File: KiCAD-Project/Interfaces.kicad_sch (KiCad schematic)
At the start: 62 parts, among them J201 XT30, J202 Conn_02x04_Odd_Even, J203 Conn_01x03_Shielded, J204 Conn_01x03_Shielded, U201 TI_TCAN337G, U202 TLE5012B_E1000, U203 MAX15062A

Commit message: fixing DRC
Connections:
- net +3V3: now also J202.8 (Pin_8); no longer J202.1 (Pin_1)
- net ENCODER_CS1: now also J202.2 (Pin_2); no longer J202.7 (Pin_7)
- net ENCODER_DATA: now also J202.6 (Pin_6); no longer J202.3 (Pin_3)
- net ENCODER_QOAD_A2: now also J202.5 (Pin_5); no longer J202.4 (Pin_4)
- net ENCODER_QOAD_B2: now also J202.3 (Pin_3); no longer J202.6 (Pin_6)
- net ENCODER_QOAD_I2: now also J202.1 (Pin_1); no longer J202.8 (Pin_8)
- net ENCODER_SCK: now also J202.4 (Pin_4); no longer J202.5 (Pin_5)
- net GNDS: now also J202.7 (Pin_7); no longer J202.2 (Pin_2)
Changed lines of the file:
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@@
   (junction (at 254 133.35) (diameter 1.016) (color 0 0 0 0))
   (junction (at 259.08 82.55) (diameter 1.016) (color 0 0 0 0))
-  (junction (at 262.89 128.27) (diameter 1.016) (color 0 0 0 0))
-  (junction (at 265.43 130.81) (diameter 1.016) (color 0 0 0 0))
+  (junction (at 262.89 130.81) (diameter 1.016) (color 0 0 0 0))
+  (junction (at 265.43 128.27) (diameter 1.016) (color 0 0 0 0))
   (junction (at 266.7 120.65) (diameter 1.016) (color 0 0 0 0))
-  (junction (at 267.97 149.86) (diameter 1.016) (color 0 0 0 0))
+  (junction (at 267.97 157.48) (diameter 1.016) (color 0 0 0 0))
   (junction (at 280.67 118.11) (diameter 1.016) (color 0 0 0 0))
   (junction (at 289.56 77.47) (diameter 1.016) (color 0 0 0 0))
@@
     (stroke (width 0) (type solid) (color 0 0 0 0))
   )
-  (wire (pts (xy 248.92 128.27) (xy 262.89 128.27))
-    (stroke (width 0) (type solid) (color 0 0 0 0))
-  )
-  (wire (pts (xy 248.92 130.81) (xy 265.43 130.81))
+  (wire (pts (xy 248.92 128.27) (xy 265.43 128.27))
+    (stroke (width 0) (type solid) (color 0 0 0 0))
+  )
+  (wire (pts (xy 248.92 130.81) (xy 262.89 130.81))
     (stroke (width 0) (type solid) (color 0 0 0 0))
   )
@@
     (stroke (width 0) (type solid) (color 0 0 0 0))
   )
+  (wire (pts (xy 260.35 149.86) (xy 270.51 149.86))
+    (stroke (width 0) (type solid) (color 0 0 0 0))
+  )
   (wire (pts (xy 261.62 82.55) (xy 259.08 82.55))
     (stroke (width 0) (type solid) (color 0 0 0 0))
   )
-  (wire (pts (xy 262.89 128.27) (xy 292.1 128.27))
-    (stroke (width 0) (type solid) (color 0 0 0 0))
-  )
-  (wire (pts (xy 262.89 154.94) (xy 262.89 128.27))
-    (stroke (width 0) (type solid) (color 0 0 0 0))
-  )
-  (wire (pts (xy 262.89 157.48) (xy 270.51 157.48))
-    (stroke (width 0) (type solid) (color 0 0 0 0))
-  )
-  (wire (pts (xy 265.43 130.81) (xy 292.1 130.81))
-    (stroke (width 0) (type solid) (color 0 0 0 0))
-  )
-  (wire (pts (xy 265.43 152.4) (xy 265.43 130.81))
+  (wire (pts (xy 262.89 130.81) (xy 292.1 130.81))
+    (stroke (width 0) (type solid) (color 0 0 0 0))
+  )
+  (wire (pts (xy 262.89 154.94) (xy 262.89 130.81))
+    (stroke (width 0) (type solid) (color 0 0 0 0))
+  )
+  (wire (pts (xy 265.43 128.27) (xy 292.1 128.27))
+    (stroke (width 0) (type solid) (color 0 0 0 0))
+  )
+  (wire (pts (xy 265.43 152.4) (xy 265.43 128.27))
     (stroke (width 0) (type solid) (color 0 0 0 0))
   )
@@
     (stroke (width 0) (type solid) (color 0 0 0 0))
   )
-  (wire (pts (xy 267.97 148.59) (xy 267.97 149.86))
-    (stroke (width 0) (type solid) (color 0 0 0 0))
-  )
-  (wire (pts (xy 267.97 149.86) (xy 267.97 160.02))
-    (stroke (width 0) (type solid) (color 0 0 0 0))
-  )
-  (wire (pts (xy 267.97 149.86) (xy 270.51 149.86))
+  (wire (pts (xy 267.97 146.05) (xy 267.97 157.48))
+    (stroke (width 0) (type solid) (color 0 0 0 0))
+  )
+  (wire (pts (xy 267.97 157.48) (xy 267.97 160.02))
+    (stroke (width 0) (type solid) (color 0 0 0 0))
+  )
+  (wire (pts (xy 267.97 157.48) (xy 270.51 157.48))
     (stroke (width 0) (type solid) (color 0 0 0 0))
   )
@@
     (stroke (width 0) (type solid) (color 0 0 0 0))
   )
-  (wire (pts (xy 284.48 149.86) (xy 283.21 149.86))
-    (stroke (width 0) (type solid) (color 0 0 0 0))
-  )
-  (wire (pts (xy 284.48 158.75) (xy 284.48 149.86))
+  (wire (pts (xy 284.48 157.48) (xy 283.21 157.48))
+    (stroke (width 0) (type solid) (color 0 0 0 0))
+  )
+  (wire (pts (xy 284.48 158.75) (xy 284.48 157.48))
     (stroke (width 0) (type solid) (color 0 0 0 0))
   )
@@
     (stroke (width 0) (type solid) (color 0 0 0 0))
   )
-  (wire (pts (xy 294.64 157.48) (xy 283.21 157.48))
+  (wire (pts (xy 294.64 149.86) (xy 283.21 149.86))
     (stroke (width 0) (type solid) (color 0 0 0 0))
   )
@@
     (effects (font (size 1.27 1.27)) (justify right))
   )
-  (hierarchical_label "ENCODER_CS1" (shape input) (at 262.89 157.48 180)
+  (hierarchical_label "ENCODER_CS1" (shape input) (at 260.35 149.86 180)
     (effects (font (size 1.27 1.27)) (justify right))
   )
-  (hierarchical_label "ENCODER_QOAD_A2" (shape input) (at 294.64 152.4 0)
+  (hierarchical_label "ENCODER_QOAD_I2" (shape input) (at 294.64 149.86 0)
     (effects (font (size 1.27 1.27)) (justify left))
   )
-  (hierarchical_label "ENCODER_QOAD_B2" (shape input) (at 294.64 154.94 0)
+  (hierarchical_label "ENCODER_QOAD_B2" (shape input) (at 294.64 152.4 0)
     (effects (font (size 1.27 1.27)) (justify left))
   )
-  (hierarchical_label "ENCODER_QOAD_I2" (shape input) (at 294.64 157.48 0)
+  (hierarchical_label "ENCODER_QOAD_A2" (shape input) (at 294.64 154.94 0)
     (effects (font (size 1.27 1.27)) (justify left))
   )
@@
     (pin "1")
   )
-  (symbol (lib_id "power:+3.3V") (at 267.97 148.59 0) (unit 1)
-    (in_bom yes) (on_board yes)
-    (property "Reference" "#PWR0211" (id 0) (at 267.97 152.4 0)
-      (effects (font (size 1.27 1.27)) hide)
-    )
-    (property "Value" "+3.3V" (id 1) (at 268.351 144.1958 0))
-    (property "Footprint" "" (id 2) (at 267.97 148.59 0)
-      (effects (font (size 1.27 1.27)) hide)
-    )
-    (property "Datasheet" "" (id 3) (at 267.97 148.59 0)
+  (symbol (lib_id "power:+3.3V") (at 267.97 146.05 0) (unit 1)
+    (in_bom yes) (on_board yes)
+    (property "Reference" "#PWR0211" (id 0) (at 267.97 149.86 0)
+      (effects (font (size 1.27 1.27)) hide)
+    )
+    (property "Value" "+3.3V" (id 1) (at 268.351 141.6558 0))
+    (property "Footprint" "" (id 2) (at 267.97 146.05 0)
+      (effects (font (size 1.27 1.27)) hide)
+    )
+    (property "Datasheet" "" (id 3) (at 267.97 146.05 0)
       (effects (font (size 1.27 1.27)) hide)
     )
@@
   (symbol (lib_id "power:GNDS") (at 321.31 54.61 0) (unit 1)
     (in_bom yes) (on_board yes) (fields_autoplaced)
-    (property "Reference" "#PWR?" (id 0) (at 321.31 60.96 0)
+    (property "Reference" "#PWR0145" (id 0) (at 321.31 60.96 0)
       (effects (font (size 1.27 1.27)) hide)
     )
@@
   (symbol (lib_id "power:GNDS") (at 321.31 76.2 0) (unit 1)
     (in_bom yes) (on_board yes) (fields_autoplaced)
-    (property "Reference" "#PWR?" (id 0) (at 321.31 82.55 0)
+    (property "Reference" "#PWR0146" (id 0) (at 321.31 82.55 0)
       (effects (font (size 1.27 1.27)) hide)
     )
@@
     (pin "SH")
   )
-  (symbol (lib_id "Connector_Generic:Conn_02x04_Odd_Even") (at 275.59 152.4 0) (unit 1)
+  (symbol (lib_id "Connector_Generic:Conn_02x04_Odd_Even") (at 278.13 152.4 0) (mirror y) (unit 1)
     (in_bom yes) (on_board yes)
     (property "Reference" "J202" (id 0) (at 276.86 145.1568 0))
-    (property "Value" "Conn_02x04_Odd_Even" (id 1) (at 274.32 147.4555 0))
-    (property "Footprint" "Connector_PinHeader_2.54mm:PinHeader_2x04_P2.54mm_Vertical_SMD" (id 2) (at 275.59 152.4 0)
-      (effects (font (size 1.27 1.27)) hide)
-    )
-    (property "Datasheet" "~" (id 3) (at 275.59 152.4 0)
-      (effects (font (size 1.27 1.27)) hide)
-    )
+    (property "Value" "Conn_02x04_Odd_Even" (id 1) (at 276.86 147.4555 0))
+    (property "Footprint" "Connector_PinHeader_2.54mm:PinHeader_2x04_P2.54mm_Vertical_SMD" (id 2) (at 278.13 152.4 0)
+      (effects (font (size 1.27 1.27)) hide)
+    )
+    (property "Datasheet" "~" (id 3) (at 278.13 152.4 0)
+      (effects (font (size 1.27 1.27)) hide)
+    )

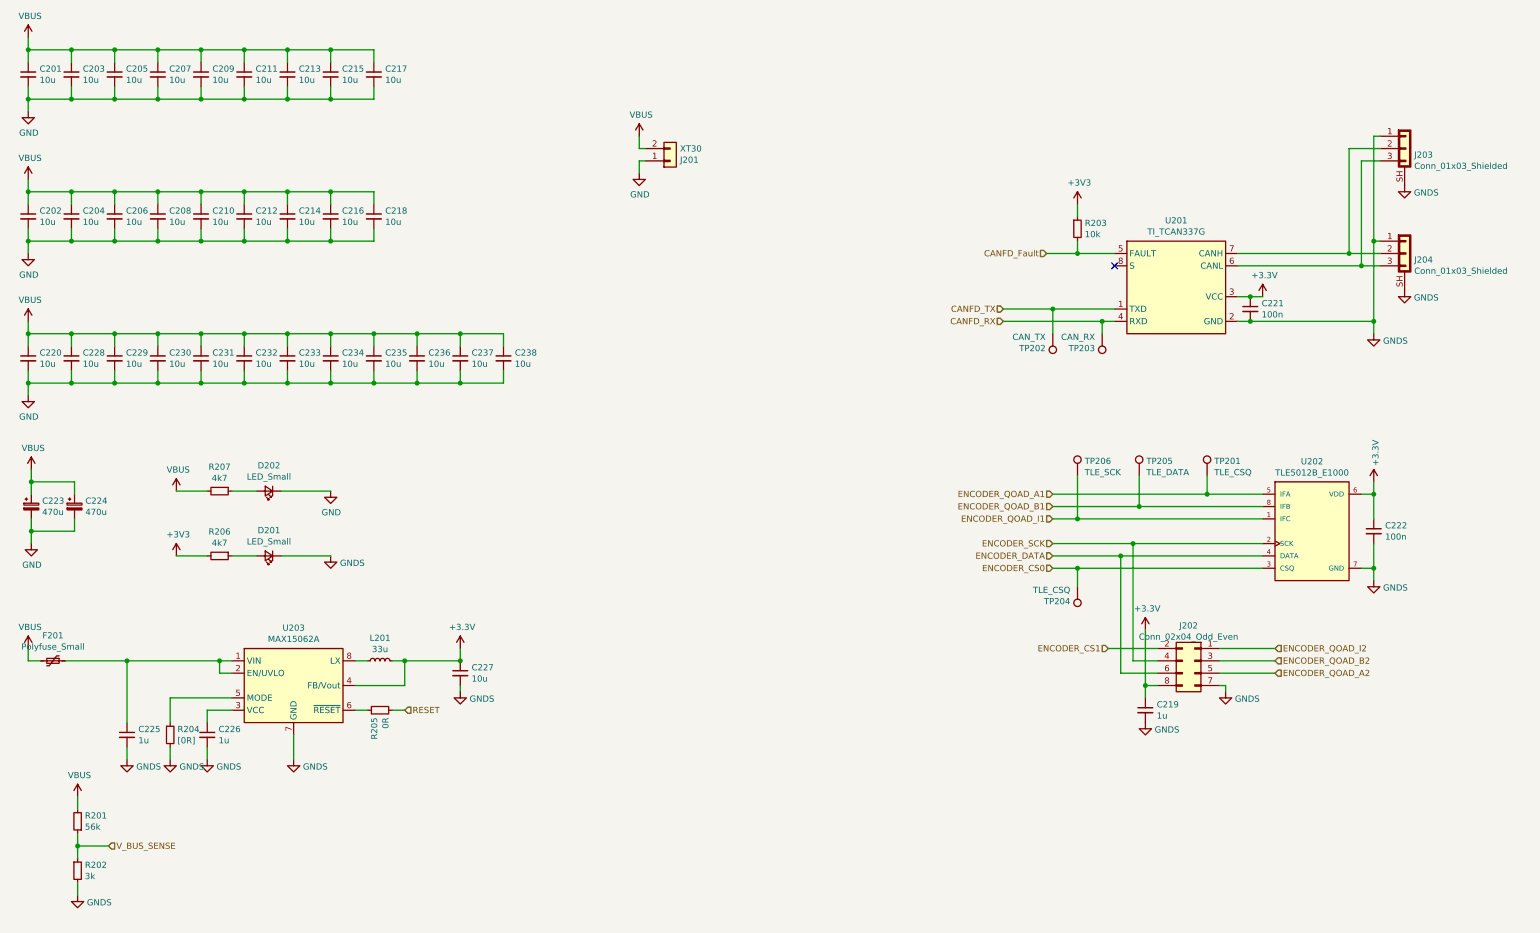
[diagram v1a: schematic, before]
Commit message: DRC resolved
removed GNDA, GNDS from schematic due to no solution was found to get a net-tie in inner layers
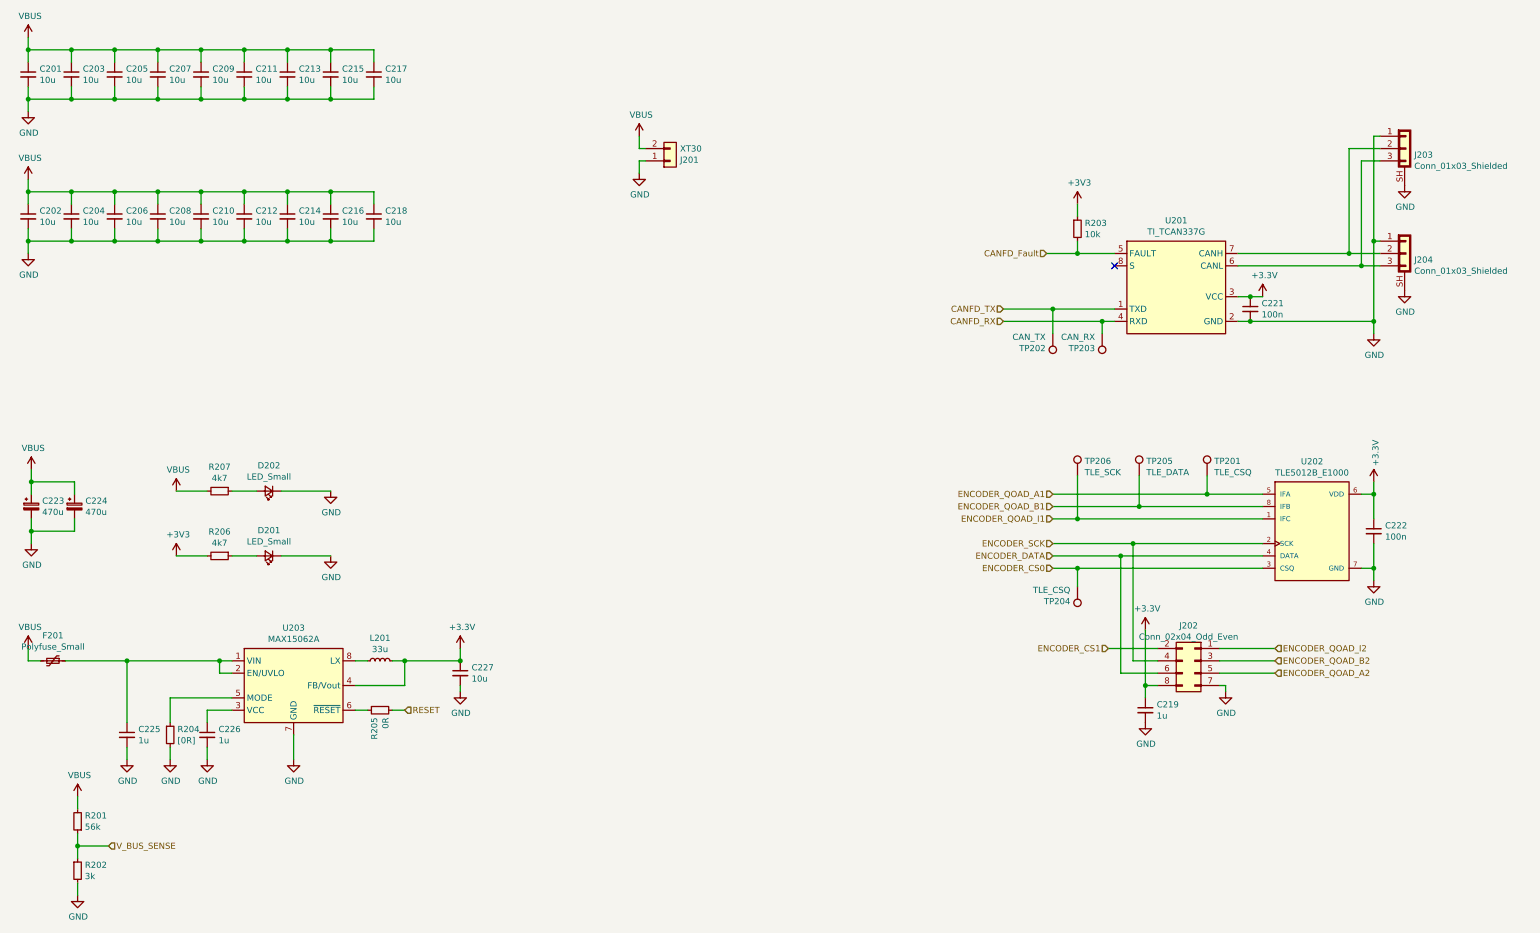
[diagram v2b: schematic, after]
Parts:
- removed C220, C228, C229, C230, C231, C232, C233, C234, C235, C236, C237, C238: 10u, Capacitor_SMD:C_1206_3216Metric, symbol Device:C_Small
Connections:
- net GNDS is gone; now on net GND: C219.2, C221.2, C222.2, C225.2, C226.2, C227.2, D201.1 (K), J202.7 (Pin_7), J203.1 (Pin_1), J203.SH (Shield), J204.1 (Pin_1), J204.SH (Shield), R202.2, R204.2, U201.2 (GND), U202.7 (GND), U203.7 (GND)

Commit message: DRC passed
1 error still reported due to placeholder in silkscreen
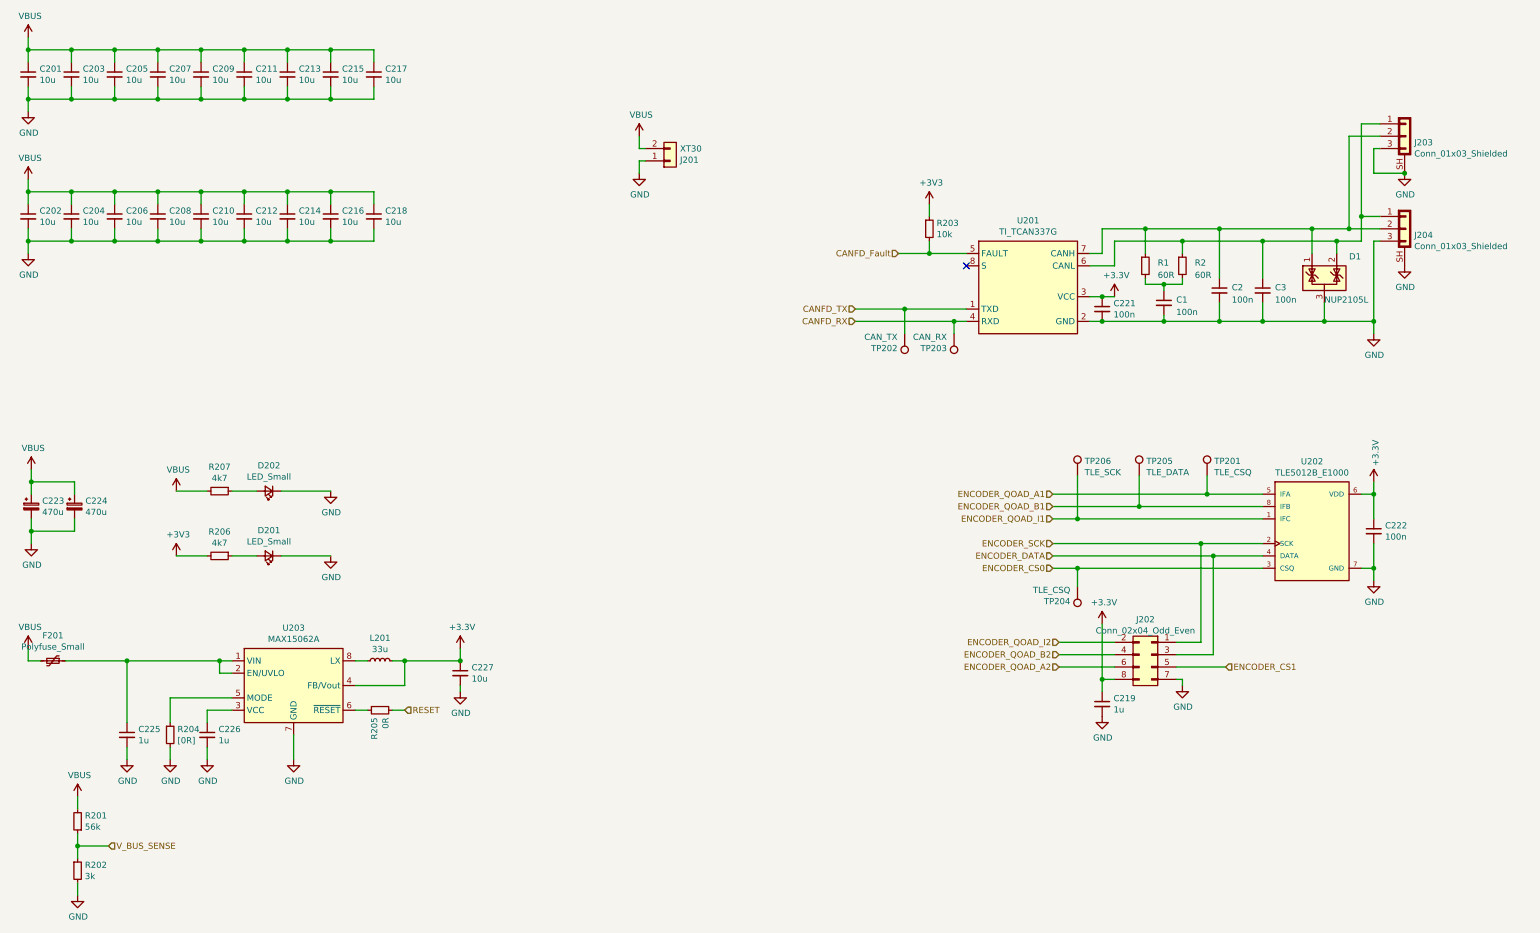
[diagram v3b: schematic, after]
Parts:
- added C1, C2, C3: 100n, Capacitor_SMD:C_0603_1608Metric, symbol Device:C_Small
- added D1: NUP2105L, Package_TO_SOT_SMD:SOT-23, symbol Power_Protection:NUP2105L
- added R1, R2: 60R, Resistor_SMD:R_0603_1608Metric, symbol Device:R_Small
- U201: footprint Package_TO_SOT_SMD:SOT-23-8_Handsoldering -> Package_SO:SOIC-8_3.9x4.9mm_P1.27mm
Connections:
- net ENCODER_CS1: now also J202.5 (Pin_5); no longer J202.2 (Pin_2)
- net ENCODER_DATA: now also J202.3 (Pin_3); no longer J202.6 (Pin_6)
- net ENCODER_QOAD_A2: now also J202.6 (Pin_6); no longer J202.5 (Pin_5)
- net ENCODER_QOAD_B2: now also J202.4 (Pin_4); no longer J202.3 (Pin_3)
- net ENCODER_QOAD_I2: now also J202.2 (Pin_2); no longer J202.1 (Pin_1)
- net ENCODER_SCK: now also J202.1 (Pin_1); no longer J202.4 (Pin_4)
- net GND: now also J203.3 (Pin_3), J204.3 (Pin_3), C1.2, C2.2, C3.2, D1.3 (A); no longer J203.1 (Pin_1), J204.1 (Pin_1)
- net at J203.2 (Pin_2), J204.2 (Pin_2), U201.7 (CANH): now also C2.1, D1.1 (K), R1.1
- new net: C3.1, D1.2 (K), J203.1 (Pin_1), J204.1 (Pin_1), R2.1, U201.6 (CANL)
- new net: C1.1, R1.2, R2.2
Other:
- moved on the sheet: C219, C221, J202, J203, J204, R203, TP202, TP203, U201
